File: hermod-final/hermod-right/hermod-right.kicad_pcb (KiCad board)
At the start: 2 copper layers, 183.9 x 155.8 mm, 212 parts, among them J1 USB_C_Receptacle_USB2.0, J2 Conn_01x05, J3 USB_C_Receptacle_USB2.0, Q1 AO3401A, Q2 MMUN2233LT1G, U1 STM32F072CBT6, U2 PRTR5V0U2X, U3 XC6206PxxxMR-Regulator_Linear, U4 CR2013-MI2120, U5 TXB0101

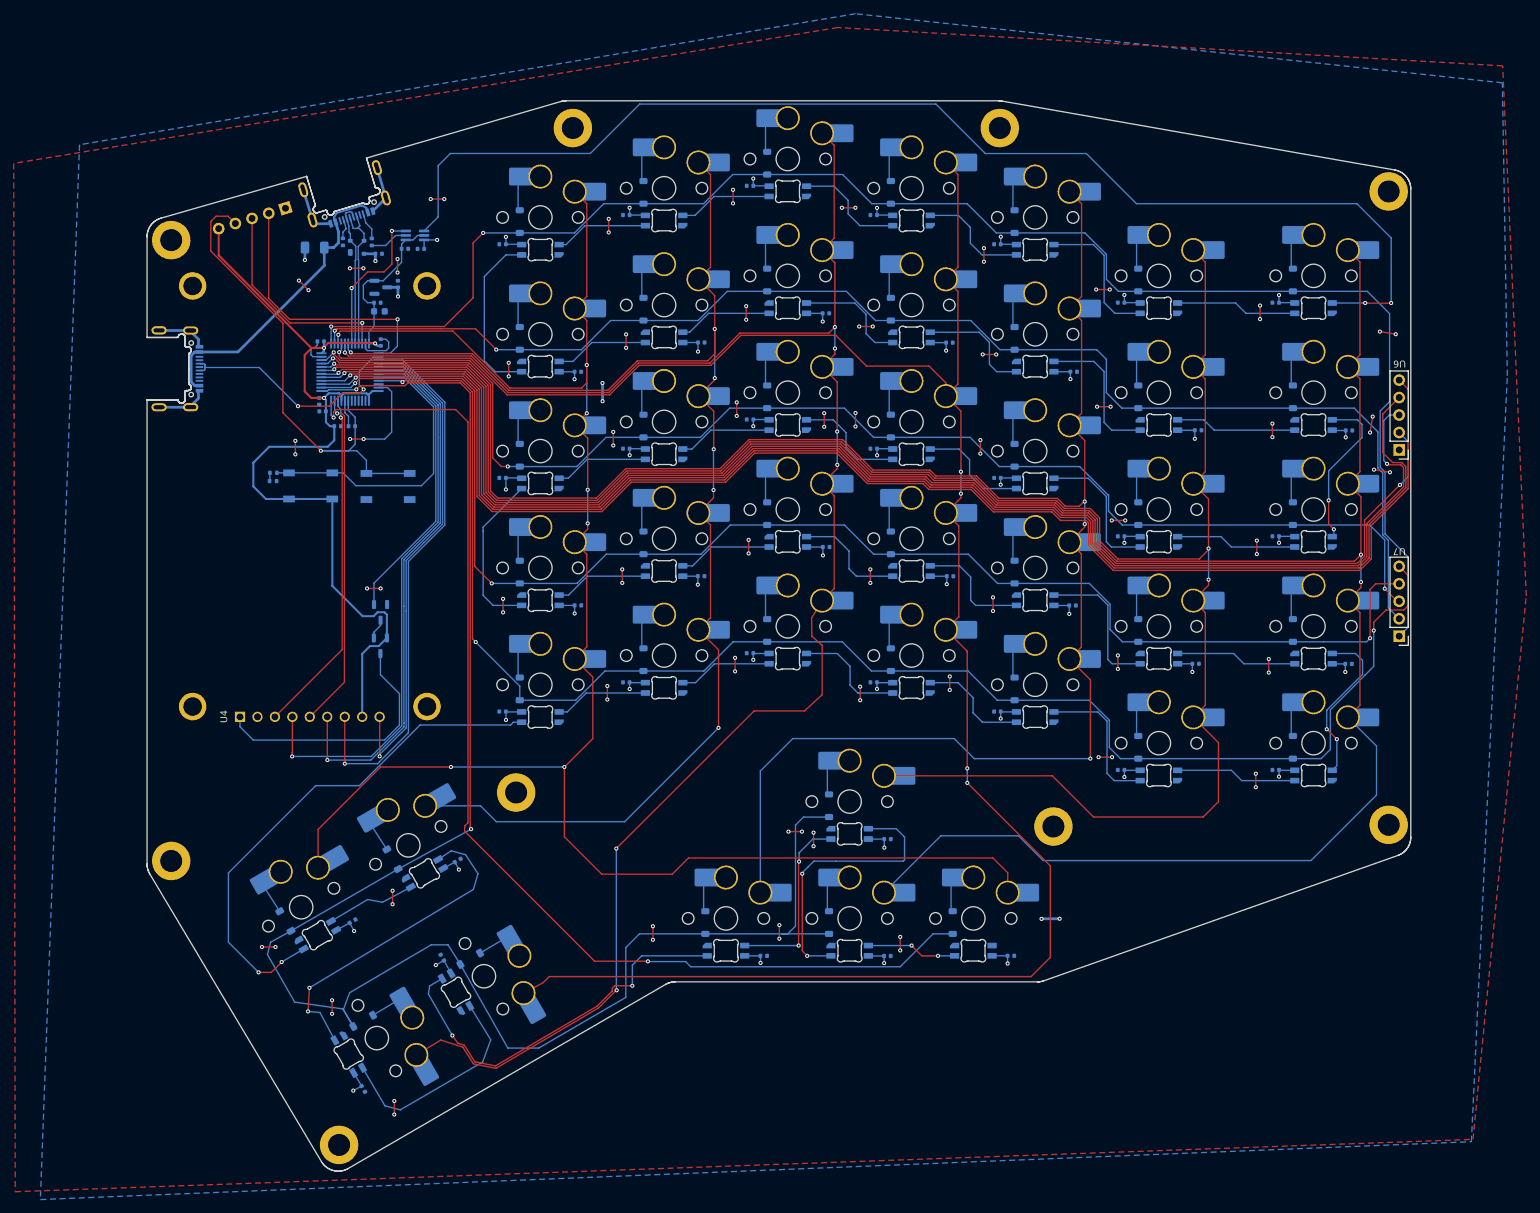
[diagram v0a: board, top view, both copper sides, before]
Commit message: Fixed random trace on numpad
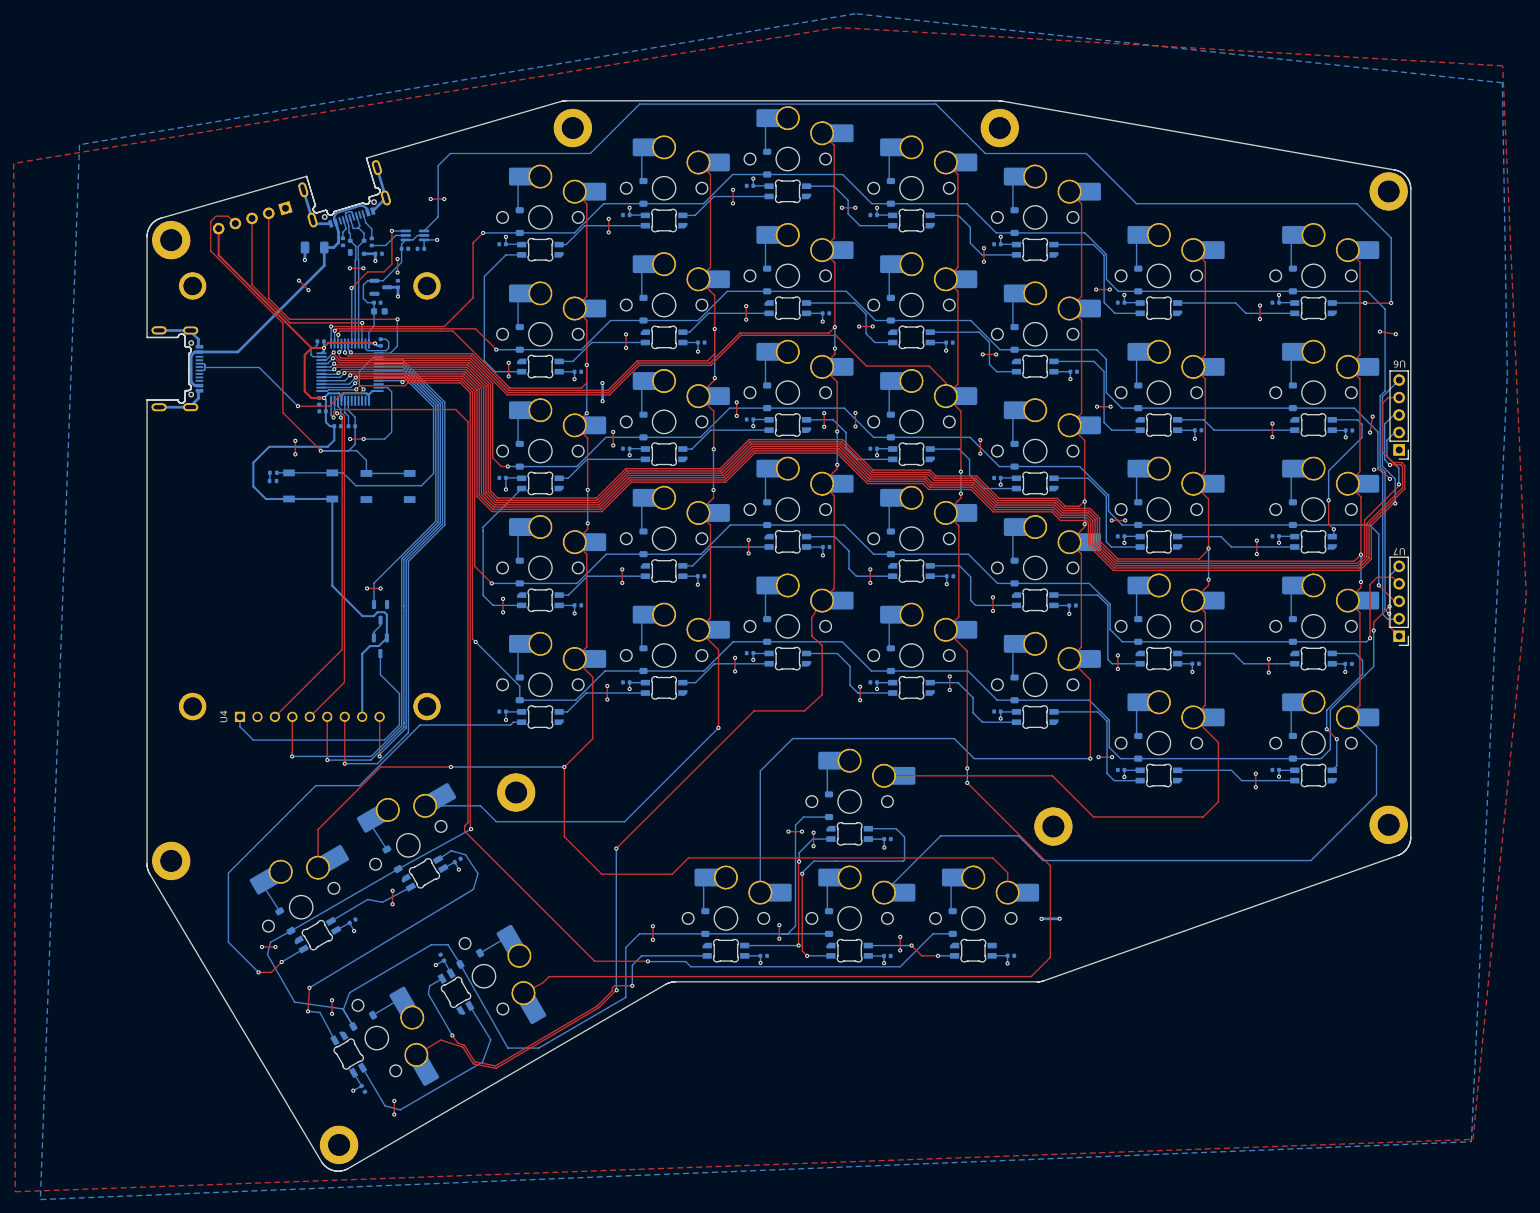
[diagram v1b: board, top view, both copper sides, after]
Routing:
- net row4: track 227.0 -> 224.4 mm, vias 3 -> 4
- net row0: track 230.6 -> 228.9 mm, vias 2 -> 3
- net row3: track 205.1 -> 206.3 mm
- net row1: track 198.4 -> 199.4 mm
- net col10: track 203.5 -> 204.4 mm
- net col8: track 211.9 -> 212.7 mm
- net col9: track 209.7 -> 208.9 mm
- net col7: track 212.5 -> 213.1 mm, vias 1 -> 2
- net GND: track 167.1 -> 167.6 mm
